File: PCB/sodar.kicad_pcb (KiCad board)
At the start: 2 copper layers, 70 parts, among them J1 Screw_Terminal_01x02, J2 Conn_02x12_Counter_Clockwise, J3 Conn_01x02, U1 TC78H621FNG, U10 TC78H621FNG, U2 TC78H621FNG, U3 TC78H621FNG, U4 TC78H621FNG, U5 TC78H621FNG, U6 TC78H621FNG, U7 TC78H621FNG, U8 TC78H621FNG, U9 TC78H621FNG

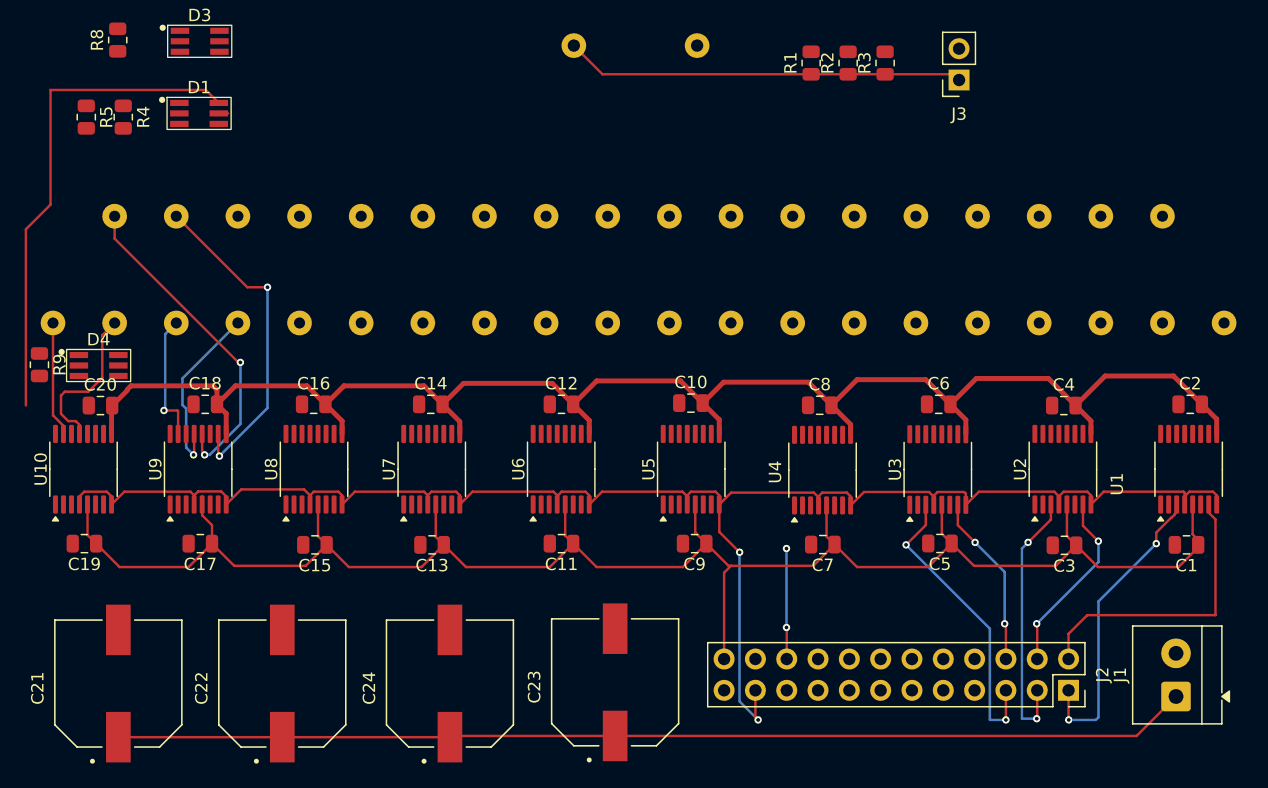
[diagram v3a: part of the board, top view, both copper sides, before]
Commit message: First version routing of EN, STBY, Transducers, 3.3V and Vdrive
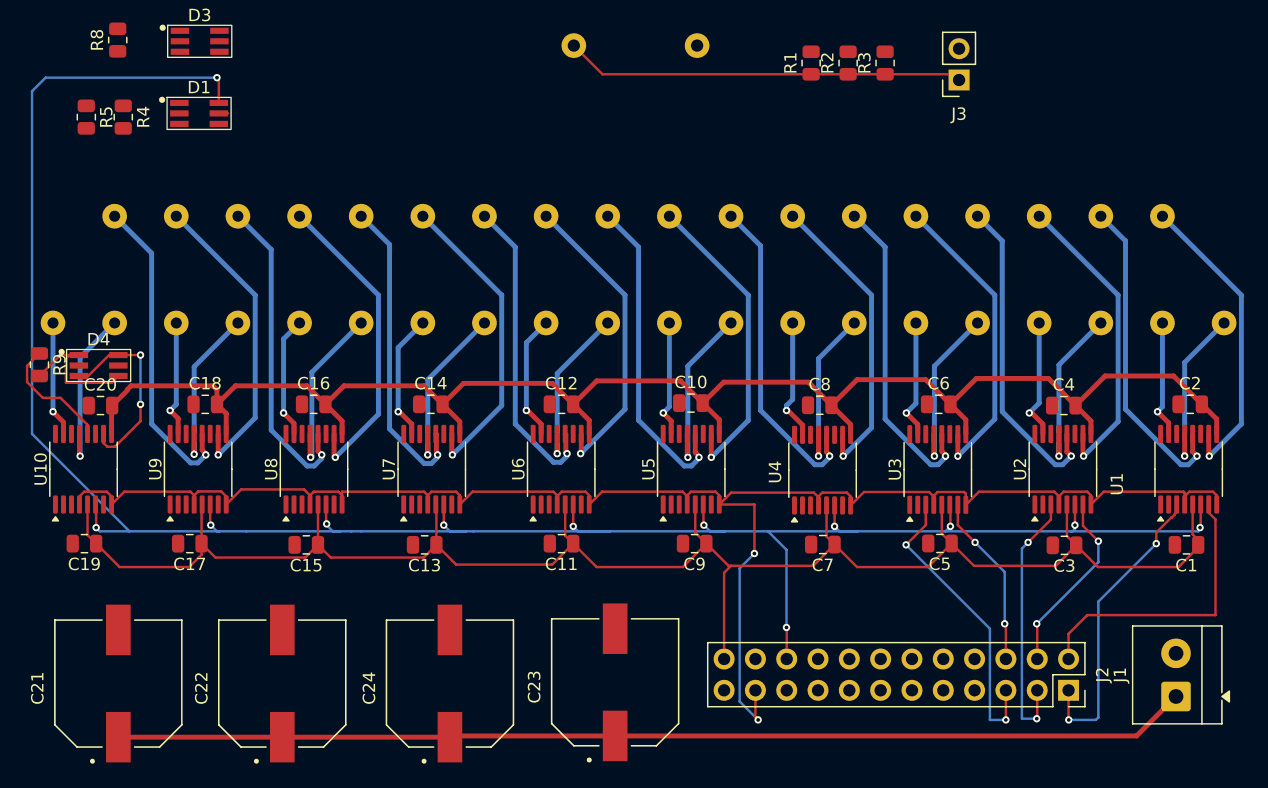
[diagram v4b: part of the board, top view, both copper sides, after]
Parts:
- moved C17 0.85 mm to (115.1, 78.9)
- moved C15 0.70 mm to (124.5, 79.0)
- moved C13 0.60 mm to (134.2, 79.0)
- turned LS11 to 0 degrees
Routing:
- net STBY: track 49.5 -> 189.0 mm, vias 2 -> 12
- net Net-(U5-BO1): track 0.00 -> 26.4 mm, vias 0 -> 1
- net Net-(U1-BO1): track 0.00 -> 26.4 mm, vias 0 -> 1
- net Net-(U4-BO1): track 0.00 -> 26.3 mm, vias 0 -> 1
- net Net-(U2-BO1): track 0.00 -> 26.3 mm, vias 0 -> 1
- net Net-(U3-BO1): track 0.00 -> 26.2 mm, vias 0 -> 1
- net Net-(U8-BO1): track 0.00 -> 26.1 mm, vias 0 -> 1
- net Net-(U8-BO2): track 0.00 -> 25.6 mm, vias 0 -> 1
- net Net-(U6-BO1): track 0.00 -> 25.4 mm, vias 0 -> 1
- net Net-(U7-BO1): track 0.00 -> 25.4 mm, vias 0 -> 1
- net Net-(U7-BO2): track 0.00 -> 25.4 mm, vias 0 -> 1
- net Net-(U5-BO2): track 0.00 -> 25.4 mm, vias 0 -> 1
- net Net-(U3-BO2): track 0.00 -> 25.3 mm, vias 0 -> 1
- net Net-(U2-BO2): track 0.00 -> 25.1 mm, vias 0 -> 1
- net Net-(U6-BO2): track 0.00 -> 25.0 mm, vias 0 -> 1
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
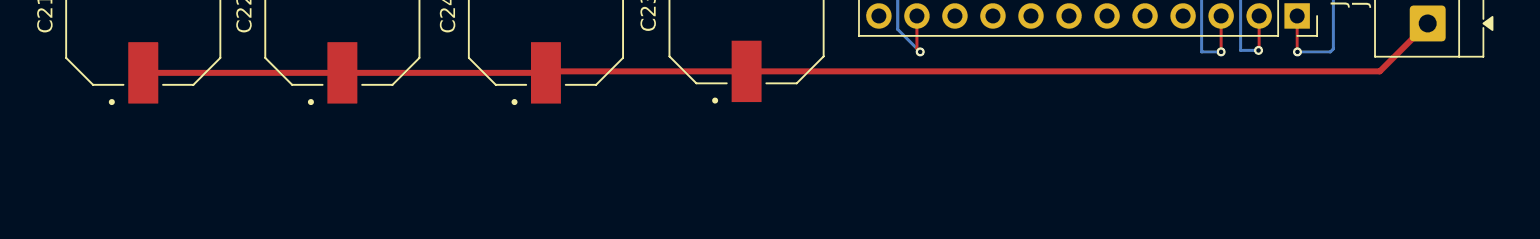
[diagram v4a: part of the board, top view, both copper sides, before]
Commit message: Added mounting holes
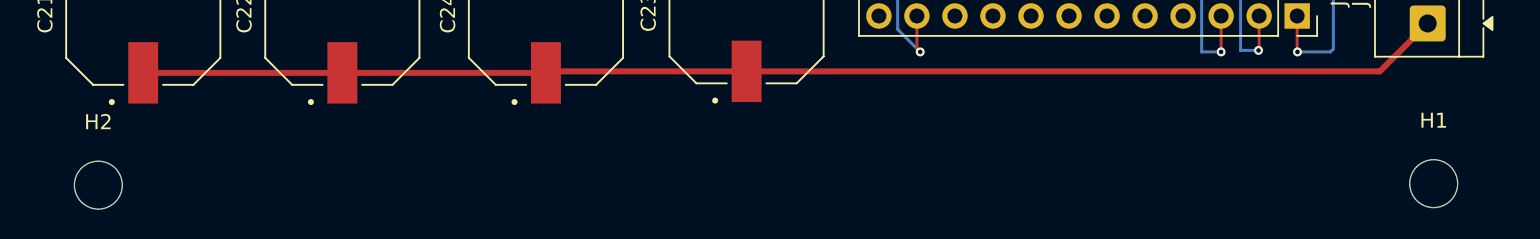
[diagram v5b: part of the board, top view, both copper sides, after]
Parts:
- added H1: MountingHole, MountingHole:MountingHole_3.2mm_M3, F.Cu at (195.5, 102.0)
- added H2: MountingHole, MountingHole:MountingHole_3.2mm_M3, F.Cu at (106.3, 102.1)

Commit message: connected all and fixed all of the errors
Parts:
- moved R9 1.31 mm to (104.2, 64.5)
- moved D4 1.20 mm to (108.9, 62.4)
- moved C9 0.90 mm to (155.2, 78.9)
- moved C3 0.80 mm to (185.2, 79.0)
- moved C11 0.60 mm to (144.7, 78.9)
- moved C1 0.45 mm to (195.5, 79.0)
- moved H2 0.32 mm to (106.6, 102.0)
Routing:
- net LED: track 0.00 -> 92.0 mm, vias 0 -> 6
- net S19: track 0.00 -> 85.4 mm, vias 0 -> 3
- net S17: track 0.00 -> 77.9 mm, vias 0 -> 2
- net GND: track 0.29 -> 66.5 mm
- net S15: track 0.00 -> 60.6 mm, vias 0 -> 4
- net +3V3: track 144.5 -> 202.6 mm, vias 0 -> 16
- net EN: track 142.7 -> 200.5 mm, vias 2 -> 12
- net S18: track 0.00 -> 56.4 mm, vias 0 -> 2
- net S13: track 0.00 -> 56.1 mm, vias 0 -> 2
- net S16: track 0.00 -> 49.8 mm, vias 0 -> 2
- net S11: track 0.00 -> 49.1 mm, vias 0 -> 2
- net S14: track 0.00 -> 43.0 mm, vias 0 -> 2
- net S9: track 0.00 -> 40.5 mm, vias 0 -> 2
- net Vdrive: track 218.5 -> 258.8 mm, vias 0 -> 2
- net S12: track 0.00 -> 34.3 mm, vias 0 -> 2
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- added copper zone on B.Cu, net GND
- added copper zone on F.Cu, net GND
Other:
- board outline added: 100 x 77.2 mm

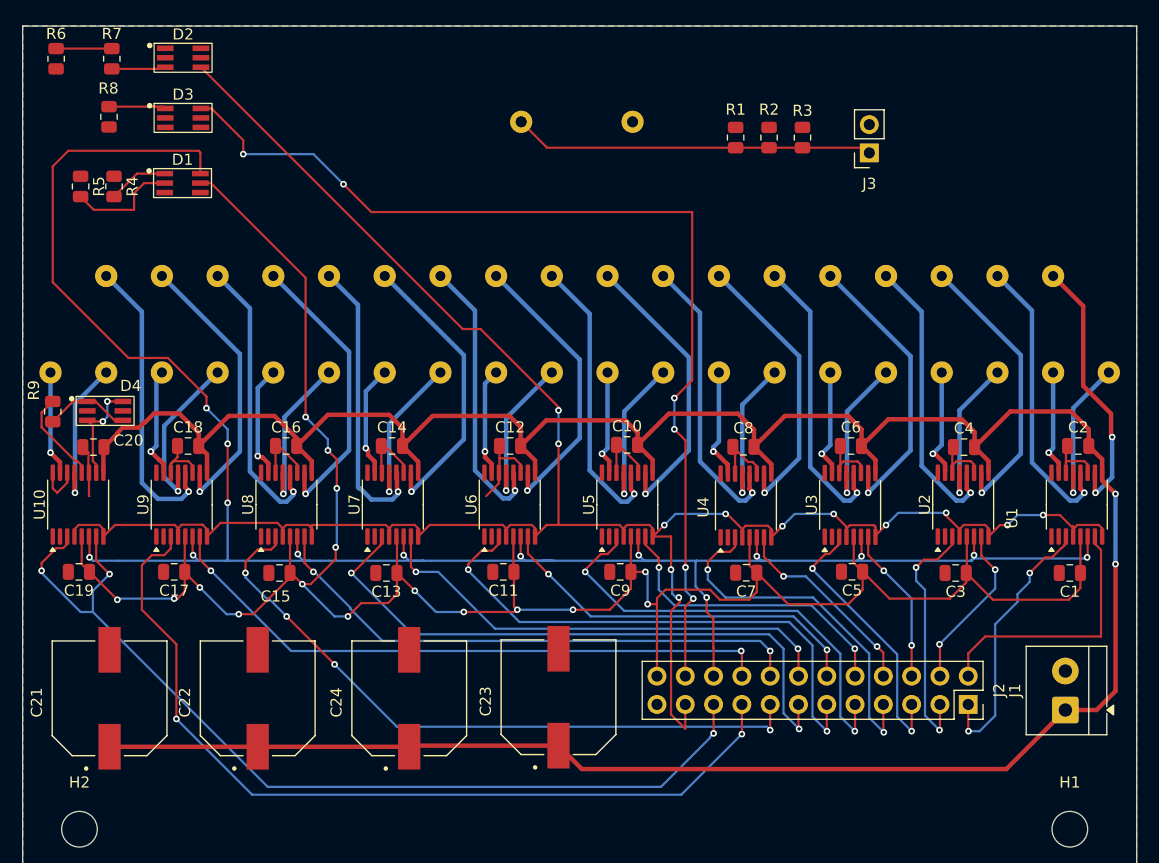
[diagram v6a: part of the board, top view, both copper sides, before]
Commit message: Changed some traces and led possiotion
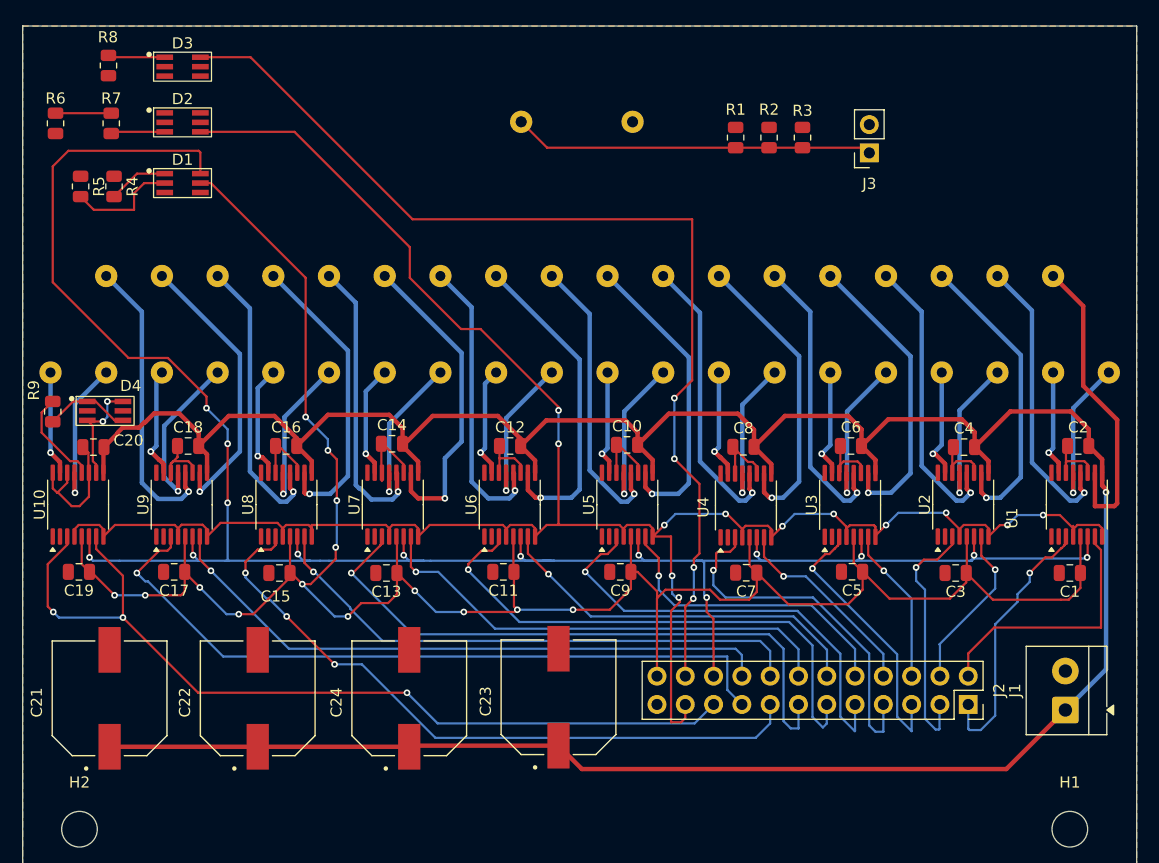
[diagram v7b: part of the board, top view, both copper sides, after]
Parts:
- moved D2 5.80 mm to (115.8, 36.5)
- moved R6 5.80 mm to (104.5, 38.6)
- moved R7 5.80 mm to (109.5, 38.6)
- moved D3 4.60 mm to (115.8, 31.4)
- moved R8 4.60 mm to (109.2, 33.5)
- moved C14 0.20 mm to (134.7, 67.4)
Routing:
- net S17: track 77.9 -> 65.9 mm, vias 2 -> 1
- net S19: track 85.4 -> 80.1 mm
- net Net-(U1-BO2): track 24.2 -> 27.9 mm, vias 2 -> 0
- net Net-(U6-BO2): track 25.9 -> 29.1 mm
- net Vdrive: track 258.8 -> 255.8 mm, vias 2 -> 1
- net Net-(U7-BO2): track 26.0 -> 28.4 mm
- net +3V3: track 202.6 -> 200.7 mm, vias 16 -> 14
- net Net-(U2-BO2): track 25.7 -> 27.3 mm
- net Net-(U4-BO2): track 25.5 -> 27.1 mm
- net Net-(U5-BO2): track 26.1 -> 27.5 mm
- net EN: track 200.5 -> 199.1 mm
- net LED: track 92.0 -> 93.3 mm, vias 6 -> 4
- net Net-(U8-BO2): track 25.9 -> 27.1 mm
- net Net-(U3-BO2): track 26.0 -> 27.2 mm
- net GND: track 66.5 -> 67.5 mm
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
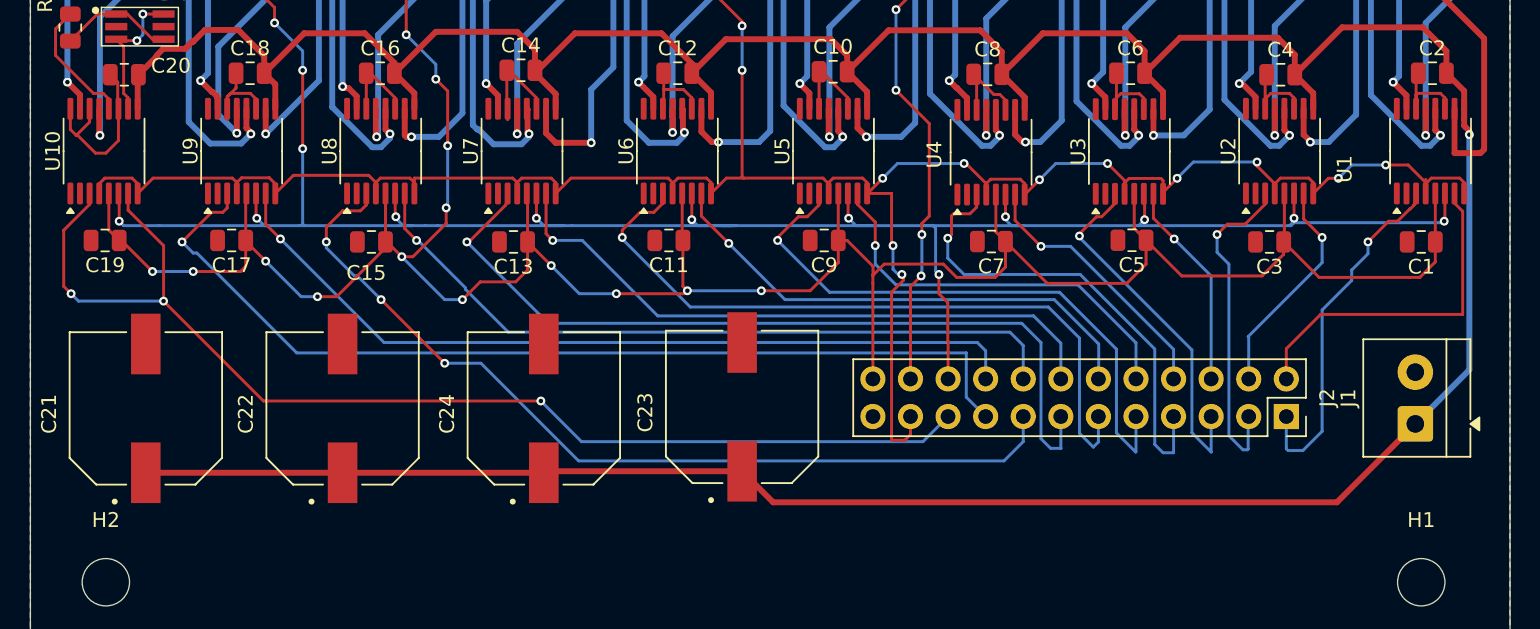
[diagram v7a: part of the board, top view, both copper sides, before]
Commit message: Added cap on 3.3V and changed the place for a vdrive and rerouted nececery things
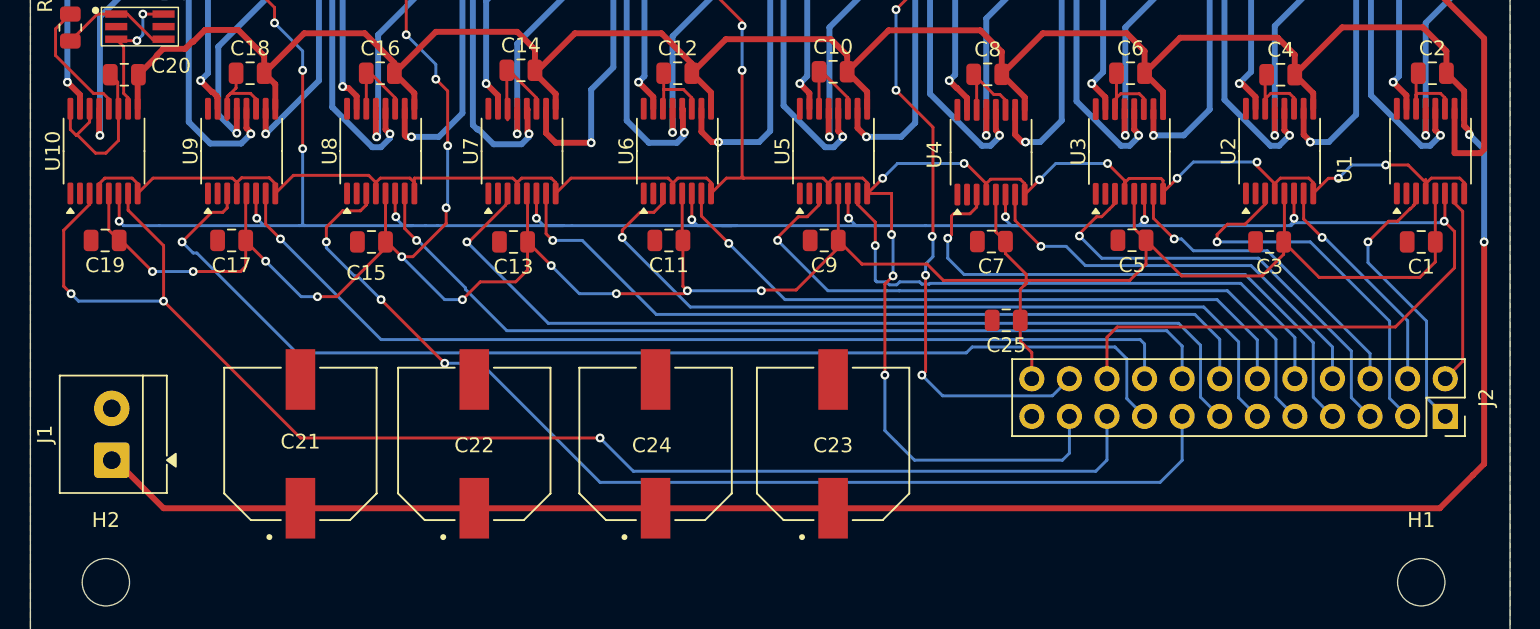
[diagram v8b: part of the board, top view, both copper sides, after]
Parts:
- added C25: 10u, Capacitor_SMD:C_0805_2012Metric, F.Cu at (167.4, 84.3)
- moved J1 88.1 mm to (107.0, 93.8)
- moved J2 10.7 mm to (197.1, 90.8)
- moved C21 10.7 mm to (119.8, 92.7)
- moved C22 9.22 mm to (131.5, 92.7)
- moved C24 7.92 mm to (143.8, 92.7)
- moved C23 6.64 mm to (155.8, 92.7)
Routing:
- net STBY: track 191.9 -> 212.3 mm, vias 14 -> 13
- net S19: track 80.1 -> 94.2 mm
- net S15: track 60.8 -> 73.5 mm
- net EN: track 199.1 -> 211.2 mm, vias 12 -> 13
- net S10: track 27.5 -> 39.3 mm
- net S18: track 56.2 -> 67.2 mm
- net S17: track 65.9 -> 76.8 mm
- net S14: track 43.0 -> 53.9 mm
- net S12: track 34.3 -> 45.2 mm
- net S8: track 18.1 -> 28.9 mm
- net S16: track 49.8 -> 60.5 mm
- net LED: track 93.3 -> 104.0 mm, vias 4 -> 5
- net S2: track 23.3 -> 13.2 mm
- net Vdrive: track 255.8 -> 263.9 mm, vias 1 -> 2
- net S6: track 14.1 -> 21.8 mm
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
